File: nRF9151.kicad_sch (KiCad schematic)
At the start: 84 parts, among them IC1 SKY65943-11, J1 SIM_Card_Shielded, J10 Conn_Coaxial, J14 Conn_01x06_Pin, J15 Conn_01x03_MountingPin, J7 Conn_Coaxial, SW3 SW_Push, U13 W25Q128JVE, U6 nRF9151-LAXX

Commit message: Update PowerLineSensorPCB and nRF9151 schematic with designator adjustments and new GND symbol
- Modified the used designators in PowerLineSensorPCB to include an additional power reference.
- Renamed the sheet in PowerLineSensorPCB for clarity.
- Removed unnecessary junctions and adjusted wire connections in nRF9151 schematic for improved layout.
- Added a new GND symbol in nRF9151 schematic to create a global label for ground.
- Adjusted positions of several components and properties for better alignment and readability.
- Updated subproject commit reference for kicad-libs.
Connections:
- net GND: now also C26.2, C27.2, C28.2, C29.2, C40.2
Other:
- moved on the sheet: L4, R127
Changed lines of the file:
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@@
 	)
 	(junction
-		(at 171.45 62.23)
+		(at 86.36 190.5)
 		(diameter 0)
 		(color 0 0 0 0)
 	)
 	(junction
-		(at 86.36 190.5)
+		(at 88.9 190.5)
 		(diameter 0)
 		(color 0 0 0 0)
 	)
 	(junction
-		(at 88.9 190.5)
+		(at 172.72 62.23)
 		(diameter 0)
 		(color 0 0 0 0)
@@
 	)
 	(junction
+		(at 17.78 33.02)
+		(diameter 0)
+		(color 0 0 0 0)
+	)
+	(junction
 		(at 215.9 62.23)
 		(diameter 0)
@@
 	)
 	(junction
-		(at 177.8 62.23)
-		(diameter 0)
-		(color 0 0 0 0)
-	)
-	(junction
 		(at 35.56 190.5)
 		(diameter 0)
@@
 	(wire
 		(pts
-			(xy 177.8 41.91) (xy 177.8 49.53)
+			(xy 172.72 41.91) (xy 172.72 49.53)
 		)
 		(stroke
@@
 	(wire
 		(pts
-			(xy 177.8 57.15) (xy 177.8 62.23)
+			(xy 172.72 57.15) (xy 172.72 62.23)
 		)
 		(stroke
@@
 	(wire
 		(pts
-			(xy 177.8 62.23) (xy 184.15 62.23)
-		)
-		(stroke
-			(width 0)
-			(type default)
-		)
-	)
-	(wire
-		(pts
 			(xy 52.07 62.23) (xy 52.07 69.85)
 		)
@@
 	(wire
 		(pts
-			(xy 171.45 72.39) (xy 171.45 76.2)
+			(xy 172.72 72.39) (xy 172.72 76.2)
 		)
 		(stroke
@@
 	(wire
 		(pts
-			(xy 171.45 62.23) (xy 177.8 62.23)
-		)
-		(stroke
-			(width 0)
-			(type default)
-		)
-	)
-	(wire
-		(pts
 			(xy 67.31 24.13) (xy 67.31 25.4)
 		)
@@
 	(wire
 		(pts
+			(xy 172.72 62.23) (xy 184.15 62.23)
+		)
+		(stroke
+			(width 0)
+			(type default)
+		)
+	)
+	(wire
+		(pts
 			(xy 33.02 190.5) (xy 35.56 190.5)
 		)
@@
 	(wire
 		(pts
-			(xy 168.91 62.23) (xy 171.45 62.23)
+			(xy 168.91 62.23) (xy 172.72 62.23)
 		)
 		(stroke
@@
 	(wire
 		(pts
-			(xy 171.45 64.77) (xy 171.45 62.23)
+			(xy 172.72 64.77) (xy 172.72 62.23)
 		)
 		(stroke
@@
 	(wire
 		(pts
-			(xy 177.8 41.91) (xy 186.69 41.91)
+			(xy 172.72 41.91) (xy 186.69 41.91)
 		)
 		(stroke
@@
 	(wire
 		(pts
+			(xy 17.78 33.02) (xy 17.78 34.29)
+		)
+		(stroke
+			(width 0)
+			(type default)
+		)
+	)
+	(wire
+		(pts
 			(xy 181.61 102.87) (xy 185.42 102.87)
 		)
@@
 	(symbol
 		(lib_id "Device:R")
-		(at 177.8 53.34 0)
+		(at 172.72 53.34 0)
 		(unit 1)
 		(body_style 1)
@@
 		(dnp yes)
 		(property "Reference" "R127"
-			(at 172.974 53.34 90)
+			(at 167.894 53.34 90)
 			(show_name no)
 			(do_not_autoplace no)
@@
 		)
 		(property "Value" "0R"
-			(at 174.498 53.594 90)
+			(at 169.418 53.594 90)
 			(show_name no)
 			(do_not_autoplace no)
@@
 		)
 		(property "Footprint" "Resistor_SMD:R_0402_1005Metric"
-			(at 176.022 53.34 90)
+			(at 170.942 53.34 90)
 			(hide yes)
 			(show_name no)
@@
 		)
 		(property "Datasheet" ""
-			(at 177.8 53.34 0)
+			(at 172.72 53.34 0)
 			(hide yes)
 			(show_name no)
@@
 		)
 		(property "Description" "Resistor"
-			(at 177.8 53.34 0)
+			(at 172.72 53.34 0)
 			(hide yes)
 			(show_name no)
@@
 		)
 		(property "PartNumber" ""
-			(at 177.8 53.34 90)
+			(at 172.72 53.34 90)
 			(hide yes)
 			(show_name no)
@@
 		)
 		(property "KLC_S4.2_DVDD" ""
-			(at 177.8 53.34 90)
+			(at 172.72 53.34 90)
 			(hide yes)
 			(show_name no)
@@
 		)
 		(property "KLC_S4.2_VREG_LX" ""
-			(at 177.8 53.34 90)
+			(at 172.72 53.34 90)
 			(hide yes)
 			(show_name no)
@@
 		)
 		(property "KLC_S3.3" ""
-			(at 177.8 53.34 90)
+			(at 172.72 53.34 90)
 			(hide yes)
 			(show_name no)
@@
 		)
 		(property "KLC_S4.1" ""
-			(at 177.8 53.34 90)
+			(at 172.72 53.34 90)
 			(hide yes)
 			(show_name no)
@@
 	(symbol
 		(lib_id "power:GND")
+		(at 17.78 34.29 0)
+		(mirror y)
+		(unit 1)
+		(body_style 1)
+		(exclude_from_sim no)
+		(in_bom yes)
+		(on_board yes)
+		(in_pos_files yes)
+		(dnp no)
+		(fields_autoplaced yes)
+		(property "Reference" "#PWR0156"
+			(at 17.78 40.64 0)
+			(hide yes)
+			(show_name no)
+			(do_not_autoplace no)
+			(effects
+				(font
+					(size 1.27 1.27)
+				)
+			)
+		)
+		(property "Value" "GND"
+			(at 20.32 35.5599 0)
+			(show_name no)
+			(do_not_autoplace no)
+			(effects
+				(font
+					(size 1.27 1.27)
+				)
+				(justify right)
+			)
+		)
+		(property "Footprint" ""
+			(at 17.78 34.29 0)
+			(hide yes)
+			(show_name no)
+			(do_not_autoplace no)
+			(effects
+				(font
+					(size 1.27 1.27)
+				)
+			)
+		)
+		(property "Datasheet" ""
+			(at 17.78 34.29 0)
+			(hide yes)
+			(show_name no)
+			(do_not_autoplace no)
+			(effects
+				(font
+					(size 1.27 1.27)
+				)
+			)
+		)
+		(property "Description" "Power symbol creates a global label with name \"GND\" , ground"
+			(at 17.78 34.29 0)
+			(hide yes)
+			(show_name no)
+			(do_not_autoplace no)
+			(effects
+				(font
+					(size 1.27 1.27)
+				)
+			)
+		)
+		(pin "1"
+		)
+		(instances
+			(project "PowerLineSensorPCB"
+				(path "/6b3d7a89-016e-44cc-aa76-b24fbbba08cf/32a23ef1-7c62-41c9-b51f-f71bd9f490a2"
+					(reference "#PWR0156")
+					(unit 1)
+				)
+			)
+		)
+	)
+	(symbol
+		(lib_id "power:GND")
 		(at 273.05 121.92 0)
 		(mirror y)
@@
 	(symbol
 		(lib_id "power:GND")
-		(at 171.45 76.2 0)
+		(at 172.72 76.2 0)
 		(mirror y)
 		(unit 1)
@@
 		(dnp no)
 		(property "Reference" "#PWR0111"
-			(at 171.45 82.55 0)
+			(at 172.72 82.55 0)
 			(hide yes)
 			(show_name no)
@@
 		)
 		(property "Value" "GND"
-			(at 172.466 76.2 0)
+			(at 173.736 76.2 0)
 			(show_name no)
 			(do_not_autoplace no)
@@
 		)
 		(property "Footprint" ""
-			(at 171.45 76.2 0)
+			(at 172.72 76.2 0)
 			(hide yes)
 			(show_name no)
@@
 		)
 		(property "Datasheet" ""
-			(at 171.45 76.2 0)
+			(at 172.72 76.2 0)
 			(hide yes)
 			(show_name no)
@@
 		)
 		(property "Description" "Power symbol creates a global label with name \"GND\" , ground"
-			(at 171.45 76.2 0)
+			(at 172.72 76.2 0)
 			(hide yes)
 			(show_name no)
@@
 	(symbol
 		(lib_id "Device:L")
-		(at 171.45 68.58 0)
+		(at 172.72 68.58 0)
 		(unit 1)
 		(body_style 1)
@@
 		(fields_autoplaced yes)
 		(property "Reference" "L4"
-			(at 172.72 67.3099 0)
+			(at 173.99 67.3099 0)
 			(show_name no)
 			(do_not_autoplace no)
@@
 		)
 		(property "Value" "100nH"
-			(at 172.72 69.8499 0)
+			(at 173.99 69.8499 0)
 			(show_name no)
 			(do_not_autoplace no)
@@
 		)
 		(property "Footprint" "Inductor_SMD:L_0402_1005Metric"
-			(at 171.45 68.58 0)
+			(at 172.72 68.58 0)
 			(hide yes)
 			(show_name no)
@@
 		)
 		(property "Datasheet" ""
-			(at 171.45 68.58 0)
+			(at 172.72 68.58 0)
 			(hide yes)
 			(show_name no)
@@
 		)
 		(property "Description" "Inductor"
-			(at 171.45 68.58 0)
+			(at 172.72 68.58 0)
 			(hide yes)
 			(show_name no)
@@
 		)
 		(property "PartNumber" "LQW15ANR10J00D"
-			(at 171.45 68.58 0)
+			(at 172.72 68.58 0)
 			(hide yes)
 			(show_name no)

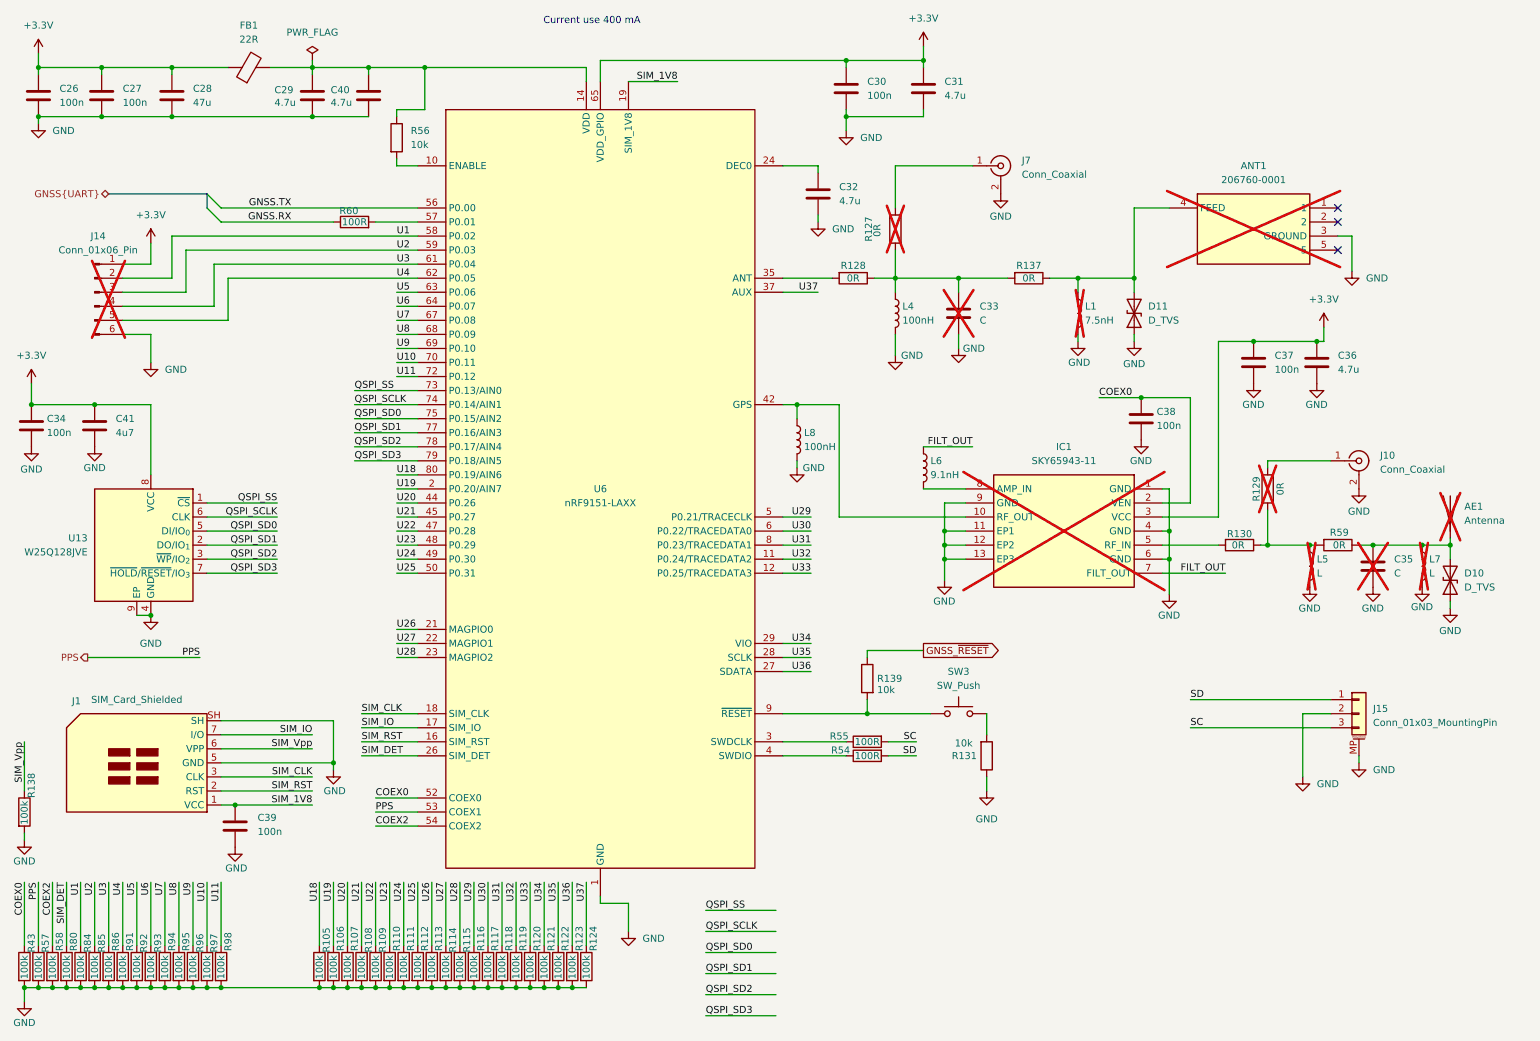
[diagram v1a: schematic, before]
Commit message: Update schematic components and properties across multiple files
- Changed capacitor values from "4.7u" to "4u7" and updated footprints from "C_0402_1005Metric" to "C_1206_3216Metric" in accelerometer.kicad_sch and nRF9151.kicad_sch.
- Updated part numbers for capacitors in accelerometer.kicad_sch and nRF9151.kicad_sch.
- Added a new resistor (R99) with value "100R" in hall_effect_sensor.kicad_sch.
- Removed unnecessary junctions in nRF9151.kicad_sch and adjusted wire connections.
- Added properties for MLX90637 and ZTPD2210 sensors in temp_sensors.kicad_sch.
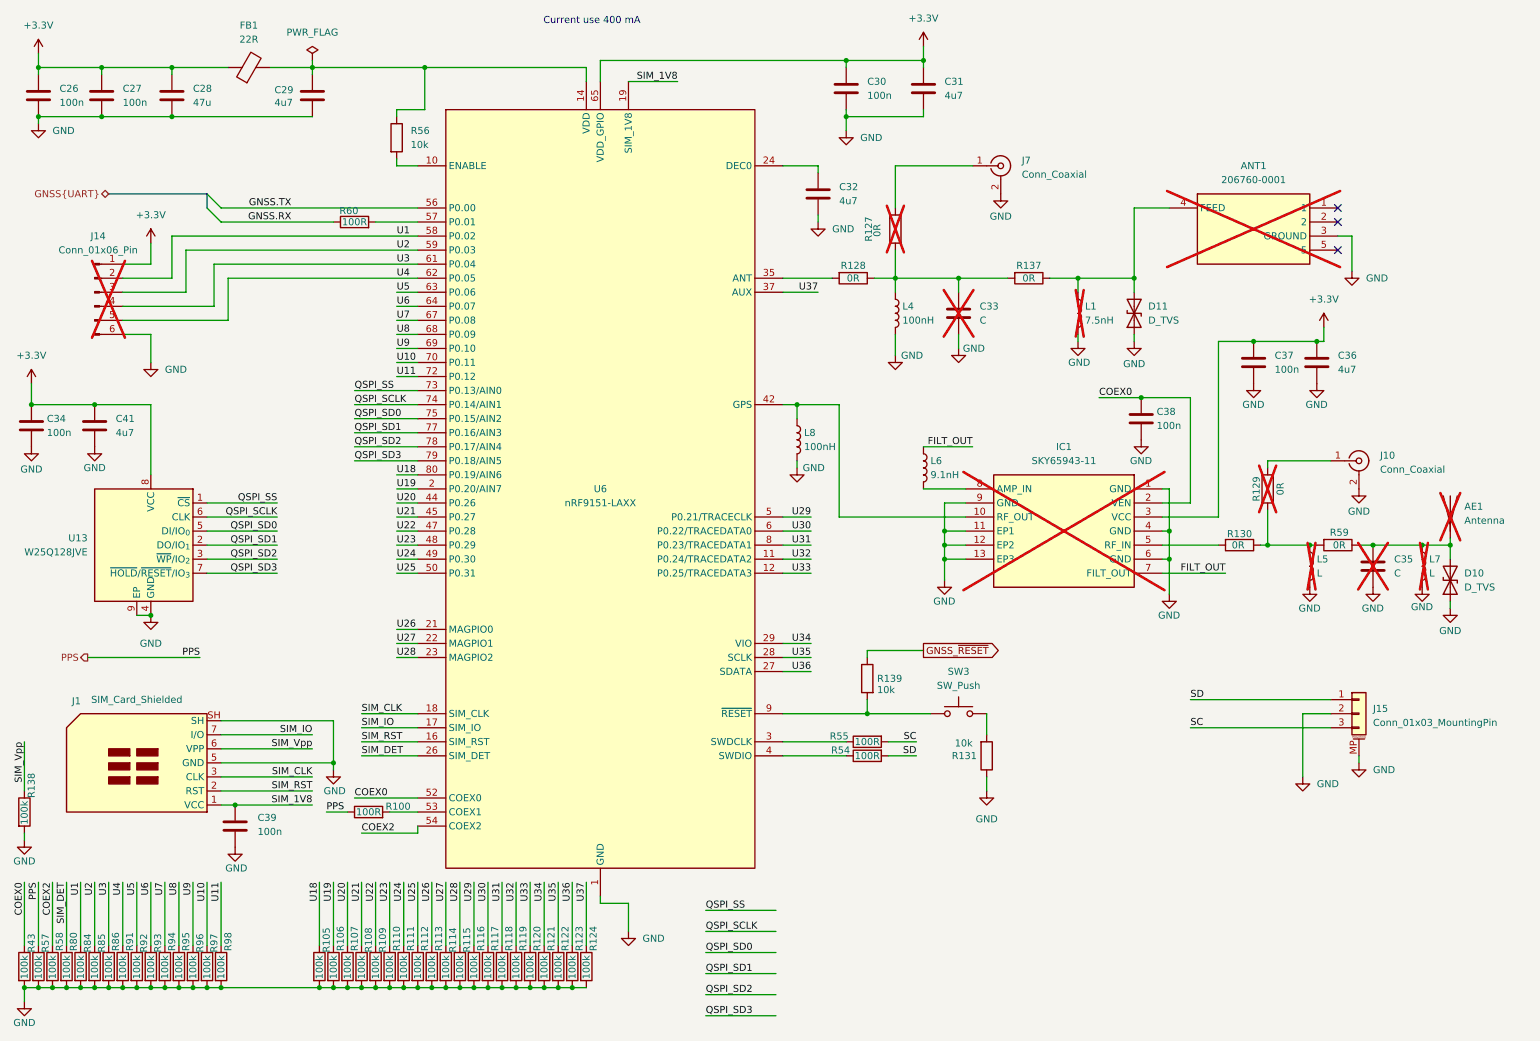
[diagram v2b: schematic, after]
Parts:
- removed C40: 4.7u, Capacitor_SMD:C_0402_1005Metric, symbol Device:C
- added R100: 100R, Resistor_SMD:R_0402_1005Metric, symbol Device:R
- ANT1: PartNumber (none) -> 206760-0001
- C28: footprint Capacitor_SMD:C_0402_1005Metric -> Capacitor_SMD:C_1206_3216Metric; PartNumber CL05B104KO5NNNC -> CL31A476MPHNNNE
- C29, C31, C32, C36: value 4.7u -> 4u7; footprint Capacitor_SMD:C_0402_1005Metric -> Capacitor_SMD:C_1206_3216Metric; PartNumber CL05B104KO5NNNC -> 1206B475K500NT
- IC1: PartNumber (none) -> SKY65943-11
- U6: PartNumber (none) -> nRF9151-A1
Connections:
- net PPS: now also R100.1; no longer U6.53 (COEX1)
- new net: R100.2, U6.53 (COEX1)

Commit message: PCB routing.
Add netclass flags for power and signal in various schematics; update capacitor footprints and part numbers

- Introduced multiple netclass flags for "Power" and "Signal" in USB_Power, hall_effect_sensor, and nRF9151 schematics to enhance clarity and organization.
- Updated capacitor footprints from "C_1206_3216Metric" to "C_0402_1005Metric" and part numbers from "1206B475K500NT" to "CL05A475MP5NRNC" in accelerometer and nRF9151 schematics for consistency and accuracy.
- Updated submodule reference in kicad-libs to ensure compatibility with the latest library changes.
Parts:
- C29, C31, C32, C36, C41: footprint Capacitor_SMD:C_1206_3216Metric -> Capacitor_SMD:C_0402_1005Metric; PartNumber 1206B475K500NT -> CL05A475MP5NRNC
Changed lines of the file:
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@@
 		(length 2.54)
 		(shape round)
+		(at 93.98 24.13 0)
+		(fields_autoplaced yes)
+		(effects
+			(font
+				(size 1.27 1.27)
+			)
+			(justify left bottom)
+		)
+		(property "Netclass" "Power"
+			(at 94.5896 21.59 0)
+			(show_name no)
+			(do_not_autoplace no)
+			(effects
+				(font
+					(size 1.27 1.27)
+				)
+				(justify left)
+			)
+		)
+		(property "Component Class" ""
+			(at 74.93 8.89 0)
+			(show_name no)
+			(do_not_autoplace no)
+			(effects
+				(font
+					(size 1.27 1.27)
+					(italic yes)
+				)
+				(justify left)
+			)
+		)
+	)
+	(netclass_flag ""
+		(length 2.54)
+		(shape round)
 		(at 203.2 62.23 0)
 		(fields_autoplaced yes)
@@
 			)
 		)
-		(property "Footprint" "Capacitor_SMD:C_1206_3216Metric"
+		(property "Footprint" "Capacitor_SMD:C_0402_1005Metric"
 			(at 178.7652 31.75 0)
 			(hide yes)
@@
 			)
 		)
-		(property "PartNumber" "1206B475K500NT"
+		(property "PartNumber" "CL05A475MP5NRNC"
 			(at 177.8 27.94 0)
 			(hide yes)
@@
 			)
 		)
-		(property "Footprint" "Capacitor_SMD:C_1206_3216Metric"
+		(property "Footprint" "Capacitor_SMD:C_0402_1005Metric"
 			(at 68.2752 33.02 0)
 			(hide yes)
@@
 			)
 		)
-		(property "PartNumber" "1206B475K500NT"
+		(property "PartNumber" "CL05A475MP5NRNC"
 			(at 67.31 29.21 0)
 			(hide yes)
@@
 			)
 		)
-		(property "Footprint" "Capacitor_SMD:C_1206_3216Metric"
+		(property "Footprint" "Capacitor_SMD:C_0402_1005Metric"
 			(at 28.9052 92.71 0)
 			(hide yes)
@@
 			)
 		)
-		(property "PartNumber" "1206B475K500NT"
+		(property "PartNumber" "CL05A475MP5NRNC"
 			(at 27.94 88.9 0)
 			(hide yes)
@@
 			)
 		)
-		(property "Footprint" "Capacitor_SMD:C_1206_3216Metric"
+		(property "Footprint" "Capacitor_SMD:C_0402_1005Metric"
 			(at 249.8852 81.28 0)
 			(hide yes)
@@
 			)
 		)
-		(property "PartNumber" "1206B475K500NT"
+		(property "PartNumber" "CL05A475MP5NRNC"
 			(at 248.92 77.47 0)
 			(hide yes)
@@
 			)
 		)
-		(property "Footprint" "Capacitor_SMD:C_1206_3216Metric"
+		(property "Footprint" "Capacitor_SMD:C_0402_1005Metric"
 			(at 159.7152 50.8 0)
 			(hide yes)
@@
 			)
 		)
-		(property "PartNumber" "1206B475K500NT"
+		(property "PartNumber" "CL05A475MP5NRNC"
 			(at 158.75 46.99 0)
 			(hide yes)

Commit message: pcb edits. remove old backups
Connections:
- net SC: now also J15.1 (Pin_1); no longer J15.3 (Pin_3)
- net SD: now also J15.3 (Pin_3); no longer J15.1 (Pin_1)
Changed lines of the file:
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@@
 		)
 	)
-	(label "SC"
+	(label "SD"
 		(at 226.06 143.51 0)
 		(effects
@@
 		)
 	)
+	(label "SC"
+		(at 226.06 138.43 0)
+		(effects
+			(font
+				(size 1.27 1.27)
+			)
+			(justify left bottom)
+		)
+	)
 	(label "U8"
 		(at 82.55 72.39 0)
@@
 		(effects
 			(font
-				(size 1.27 1.27)
-			)
-			(justify left bottom)
-		)
-	)
-	(label "SD"
-		(at 226.06 138.43 0)
-		(effects
-			(font
